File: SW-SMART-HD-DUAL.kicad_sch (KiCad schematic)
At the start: 52 parts, among them J1 SWD, J2 USART1, J3 PWRIN, SW1 BTS50010-1TAD, SW2 BTS50010-1TAD, U1 STM32G0B1KBTx, U3 LMR54410, U4 MCP2562

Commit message: lots of updates
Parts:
- CAN1: footprint TerminalBlock_TE-Connectivity:TerminalBlock_TE_282834-3_1x03_P2.54mm_Horizontal -> TerminalBlock_Phoenix:TerminalBlock_Phoenix_MPT-0,5-3-2.54_1x03_P2.54mm_Horizontal
- J3: footprint TerminalBlock_Phoenix:TerminalBlock_Phoenix_MKDS-3-2-5.08_1x02_P5.08mm_Horizontal -> TerminalBlock_Phoenix:TerminalBlock_Phoenix_MPT-0,5-2-2.54_1x02_P2.54mm_Horizontal
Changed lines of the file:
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@@
 			)
 		)
-		(property "Footprint" "TerminalBlock_TE-Connectivity:TerminalBlock_TE_282834-3_1x03_P2.54mm_Horizontal"
+		(property "Footprint" "TerminalBlock_Phoenix:TerminalBlock_Phoenix_MPT-0,5-3-2.54_1x03_P2.54mm_Horizontal"
 			(at 332.74 100.33 0)
 			(effects
@@
 			)
 		)
-		(property "Footprint" "TerminalBlock_Phoenix:TerminalBlock_Phoenix_MKDS-3-2-5.08_1x02_P5.08mm_Horizontal"
+		(property "Footprint" "TerminalBlock_Phoenix:TerminalBlock_Phoenix_MPT-0,5-2-2.54_1x02_P2.54mm_Horizontal"
 			(at 24.13 39.37 0)
 			(effects

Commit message: layout complete, drc passed
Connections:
- net SW1IS: now also U1.8 (PA1); no longer U1.7 (PA0)
- net SW2IS: now also U1.7 (PA0)
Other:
- moved on the sheet: POWER_OUT1
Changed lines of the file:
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@@
 	)
 	(junction
-		(at 198.12 153.67)
+		(at 160.02 153.67)
 		(diameter 0)
 		(color 0 0 0 0)
@@
 	)
 	(junction
-		(at 194.31 121.92)
+		(at 156.21 121.92)
 		(diameter 0)
 		(color 0 0 0 0)
@@
 	)
 	(junction
+		(at 160.02 133.35)
+		(diameter 0)
+		(color 0 0 0 0)
+	)
+	(junction
 		(at 299.72 160.02)
 		(diameter 0)
@@
 	)
 	(junction
-		(at 198.12 127)
-		(diameter 0)
-		(color 0 0 0 0)
-	)
-	(junction
 		(at 68.58 29.21)
 		(diameter 0)
@@
 	(wire
 		(pts
-			(xy 173.99 153.67) (xy 173.99 172.72)
+			(xy 160.02 153.67) (xy 160.02 172.72)
 		)
 		(stroke
@@
 	(wire
 		(pts
-			(xy 226.06 127) (xy 226.06 137.16)
+			(xy 187.96 127) (xy 187.96 137.16)
 		)
 		(stroke
@@
 	(wire
 		(pts
-			(xy 132.08 172.72) (xy 173.99 172.72)
-		)
-		(stroke
-			(width 0)
-			(type default)
-		)
-	)
-	(wire
-		(pts
 			(xy 302.26 139.7) (xy 290.83 139.7)
 		)
@@
 	(wire
 		(pts
+			(xy 289.56 48.26) (xy 293.37 48.26)
+		)
+		(stroke
+			(width 0)
+			(type default)
+		)
+	)
+	(wire
+		(pts
 			(xy 78.74 29.21) (xy 83.82 29.21)
 		)
@@
 	(wire
 		(pts
+			(xy 132.08 172.72) (xy 160.02 172.72)
+		)
+		(stroke
+			(width 0)
+			(type default)
+		)
+	)
+	(wire
+		(pts
 			(xy 62.23 21.59) (xy 53.34 21.59)
 		)
@@
 	(wire
 		(pts
-			(xy 228.6 139.7) (xy 228.6 121.92)
+			(xy 190.5 139.7) (xy 190.5 121.92)
 		)
 		(stroke
@@
 	(wire
 		(pts
-			(xy 194.31 116.84) (xy 194.31 121.92)
+			(xy 156.21 116.84) (xy 156.21 121.92)
 		)
 		(stroke
@@
 	(wire
 		(pts
-			(xy 223.52 153.67) (xy 223.52 142.24)
+			(xy 185.42 153.67) (xy 185.42 142.24)
 		)
 		(stroke
@@
 	(wire
 		(pts
-			(xy 220.98 139.7) (xy 228.6 139.7)
+			(xy 182.88 139.7) (xy 190.5 139.7)
 		)
 		(stroke
@@
 	(wire
 		(pts
+			(xy 160.02 133.35) (xy 160.02 127)
+		)
+		(stroke
+			(width 0)
+			(type default)
+		)
+	)
+	(wire
+		(pts
 			(xy 226.06 53.34) (xy 226.06 57.15)
 		)
@@
 	(wire
 		(pts
-			(xy 220.98 137.16) (xy 226.06 137.16)
+			(xy 182.88 137.16) (xy 187.96 137.16)
 		)
 		(stroke
@@
 	(wire
 		(pts
-			(xy 137.16 133.35) (xy 160.02 133.35)
-		)
-		(stroke
-			(width 0)
-			(type default)
-		)
-	)
-	(wire
-		(pts
 			(xy 68.58 35.56) (xy 68.58 60.96)
 		)
@@
 	(wire
 		(pts
-			(xy 198.12 142.24) (xy 198.12 153.67)
-		)
-		(stroke
-			(width 0)
-			(type default)
-		)
-	)
-	(wire
-		(pts
-			(xy 160.02 127) (xy 198.12 127)
+			(xy 160.02 142.24) (xy 160.02 153.67)
 		)
 		(stroke
@@
 	(wire
 		(pts
-			(xy 198.12 137.16) (xy 200.66 137.16)
+			(xy 160.02 137.16) (xy 162.56 137.16)
 		)
 		(stroke
@@
 	(wire
 		(pts
-			(xy 160.02 127) (xy 160.02 133.35)
-		)
-		(stroke
-			(width 0)
-			(type default)
-		)
-	)
-	(wire
-		(pts
 			(xy 289.56 78.74) (xy 293.37 78.74)
 		)
@@
 	(wire
 		(pts
-			(xy 173.99 153.67) (xy 198.12 153.67)
-		)
-		(stroke
-			(width 0)
-			(type default)
-		)
-	)
-	(wire
-		(pts
 			(xy 67.31 80.01) (xy 69.85 80.01)
 		)
@@
 	(wire
 		(pts
-			(xy 194.31 139.7) (xy 200.66 139.7)
+			(xy 156.21 139.7) (xy 162.56 139.7)
 		)
 		(stroke
@@
 	(wire
 		(pts
-			(xy 198.12 127) (xy 226.06 127)
+			(xy 160.02 127) (xy 187.96 127)
 		)
 		(stroke
@@
 	(wire
 		(pts
-			(xy 194.31 121.92) (xy 194.31 139.7)
+			(xy 156.21 121.92) (xy 156.21 139.7)
 		)
 		(stroke
@@
 	(wire
 		(pts
-			(xy 198.12 142.24) (xy 200.66 142.24)
+			(xy 160.02 142.24) (xy 162.56 142.24)
 		)
 		(stroke
@@
 	(wire
 		(pts
+			(xy 137.16 133.35) (xy 160.02 133.35)
+		)
+		(stroke
+			(width 0)
+			(type default)
+		)
+	)
+	(wire
+		(pts
 			(xy 46.99 128.27) (xy 52.07 128.27)
 		)
@@
 	(wire
 		(pts
-			(xy 220.98 142.24) (xy 223.52 142.24)
+			(xy 182.88 142.24) (xy 185.42 142.24)
 		)
 		(stroke
@@
 	(wire
 		(pts
-			(xy 198.12 153.67) (xy 223.52 153.67)
+			(xy 160.02 153.67) (xy 185.42 153.67)
 		)
 		(stroke
@@
 	(wire
 		(pts
-			(xy 198.12 137.16) (xy 198.12 127)
+			(xy 160.02 137.16) (xy 160.02 133.35)
 		)
 		(stroke
@@
 	(wire
 		(pts
-			(xy 228.6 121.92) (xy 194.31 121.92)
+			(xy 190.5 121.92) (xy 156.21 121.92)
 		)
 		(stroke
@@
 		)
 	)
-	(label "SW2OUT"
-		(at 173.99 157.48 0)
-		(effects
-			(font
-				(size 1.27 1.27)
-			)
-			(justify left bottom)
-		)
-	)
 	(label "SW"
 		(at 68.58 90.17 0)
@@
 	)
 	(label "SW1IS"
-		(at 293.37 45.72 0)
+		(at 293.37 48.26 0)
 		(effects
 			(font
@@
 		)
 	)
+	(label "SW2IS"
+		(at 293.37 45.72 0)
+		(effects
+			(font
+				(size 1.27 1.27)
+			)
+			(justify left bottom)
+		)
+	)
 	(label "SW1IS"
 		(at 46.99 138.43 180)
@@
 			)
 		)
-		(property "Datasheet" "https://www.infineon.com/dgdl/Infineon-BTS50010-1TAD-DS-v01_00-EN.pdf?fileId=5546d462576f34750157c38810ca55cd"
+		(property "Datasheet" "https://www.infineon.com/assets/row/public/documents/10/49/infineon-bts50010-1tad-datasheet-en.pdf"
 			(at 85.09 182.88 0)
 			(effects
@@
 			)
 		)
-		(property "Datasheet" "https://www.infineon.com/dgdl/Infineon-BTS50010-1TAD-DS-v01_00-EN.pdf?fileId=5546d462576f34750157c38810ca55cd"
+		(property "Datasheet" "https://www.infineon.com/assets/row/public/documents/10/49/infineon-bts50010-1tad-datasheet-en.pdf"
 			(at 90.17 143.51 0)
 			(effects
@@
 	(symbol
 		(lib_id "power:+12V")
-		(at 194.31 116.84 0)
+		(at 156.21 116.84 0)
 		(unit 1)
 		(exclude_from_sim no)
@@
 		(fields_autoplaced yes)
 		(property "Reference" "#PWR07"
-			(at 194.31 120.65 0)
+			(at 156.21 120.65 0)
 			(effects
 				(font
@@
 		)
 		(property "Value" "+12V"
-			(at 194.31 111.76 0)
+			(at 156.21 111.76 0)
 			(effects
 				(font
@@
 		)
 		(property "Footprint" ""
-			(at 194.31 116.84 0)
+			(at 156.21 116.84 0)
 			(effects
 				(font
@@
 		)
 		(property "Datasheet" ""
-			(at 194.31 116.84 0)
+			(at 156.21 116.84 0)
 			(effects
 				(font
@@
 		)
 		(property "Description" "Power symbol creates a global label with name \"+12V\""
-			(at 194.31 116.84 0)
+			(at 156.21 116.84 0)
 			(effects
 				(font
@@
 	(symbol
 		(lib_id "SamacSys_Parts:VP0365840000G")
-		(at 220.98 142.24 180)
+		(at 182.88 142.24 180)
 		(unit 1)
 		(exclude_from_sim no)
@@
 		(fields_autoplaced yes)
 		(property "Reference" "POWER_OUT1"
-			(at 210.82 129.54 0)
+			(at 172.72 129.54 0)
 			(effects
 				(font
@@
 		)
 		(property "Value" "VP0365840000G"
-			(at 210.82 132.08 0)
+			(at 172.72 132.08 0)
 			(effects
 				(font
@@
 		)
 		(property "Footprint" "VP0365840000G"
-			(at 204.47 47.32 0)
+			(at 166.37 47.32 0)
 			(effects
 				(font
@@
 		)
 		(property "Datasheet" "https://www.mouser.ca/ProductDetail/Amphenol-Anytek/VP0365840000G?qs=Mv7BduZupUgzoCVpYg1nQw%3D%3D"
-			(at 204.47 -52.68 0)
+			(at 166.37 -52.68 0)
 			(effects
 				(font
@@
 		)
 		(property "Description" "3 Position Wire to Board Terminal Block Horizontal with Board 0.400\" (10.16mm) Through Hole"
-			(at 220.98 142.24 0)
+			(at 182.88 142.24 0)
 			(effects
 				(font
@@
 		)
 		(property "Height" "28.8"
-			(at 204.47 -252.68 0)
+			(at 166.37 -252.68 0)
 			(effects
 				(font
@@
 		)
 		(property "Mouser Part Number" "649-VP03658400J0G"
-			(at 204.47 -352.68 0)
+			(at 166.37 -352.68 0)
 			(effects
 				(font
@@
 		)
 		(property "Mouser Price/Stock" "https://www.mouser.co.uk/ProductDetail/Amphenol-Anytek/VP0365840000G?qs=Mv7BduZupUgzoCVpYg1nQw%3D%3D"
-			(at 204.47 -452.68 0)
+			(at 166.37 -452.68 0)
 			(effects
 				(font
@@
 		)
 		(property "Manufacturer_Name" "Amphenol"
-			(at 204.47 -552.68 0)
+			(at 166.37 -552.68 0)
 			(effects
 				(font
@@
 		)
 		(property "Manufacturer_Part_Number" "VP0365840000G"
-			(at 204.47 -652.68 0)
+			(at 166.37 -652.68 0)
 			(effects
 				(font

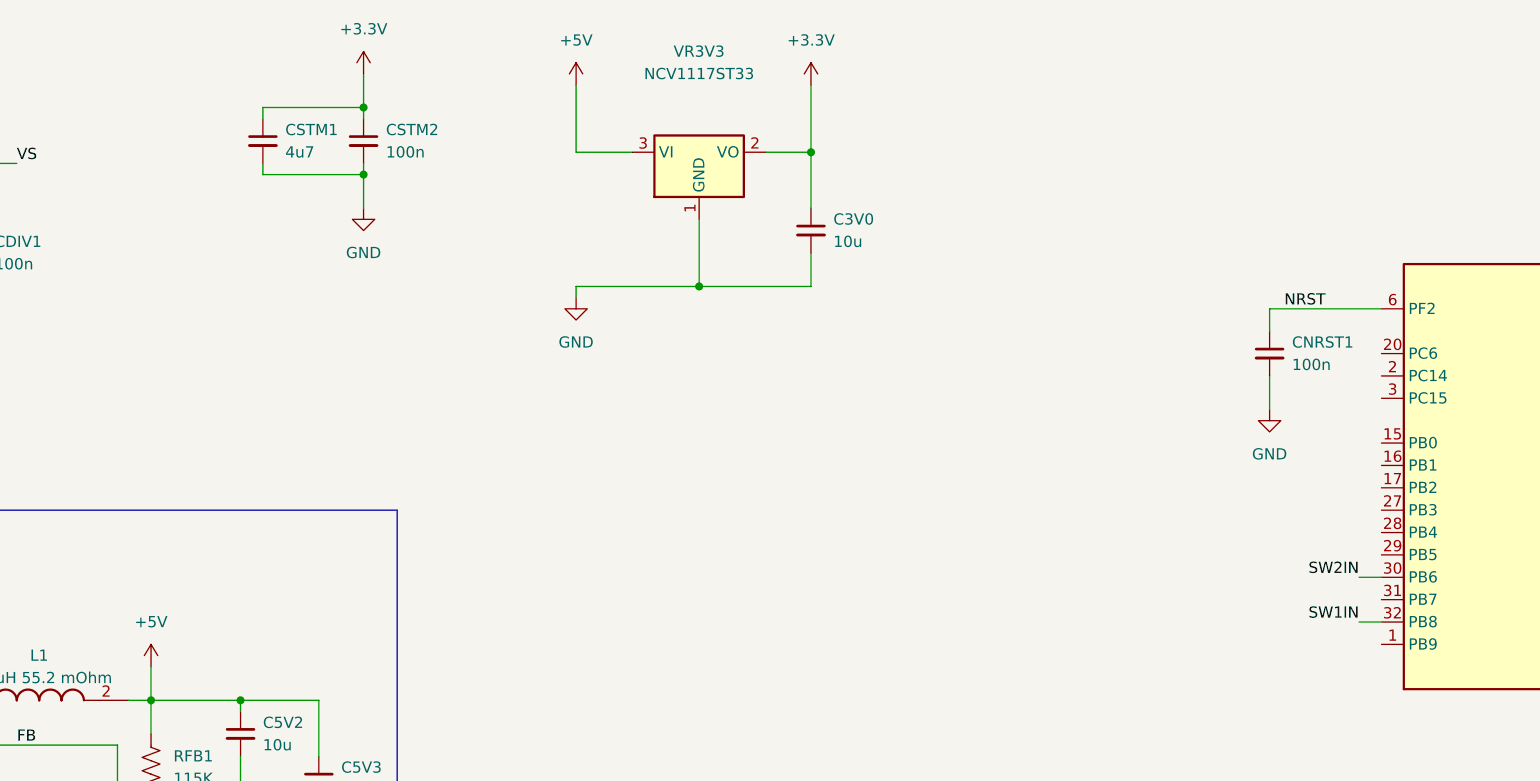
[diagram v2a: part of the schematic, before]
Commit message: added crystal osc, fixed some silkscreen issues, moved a few tracks
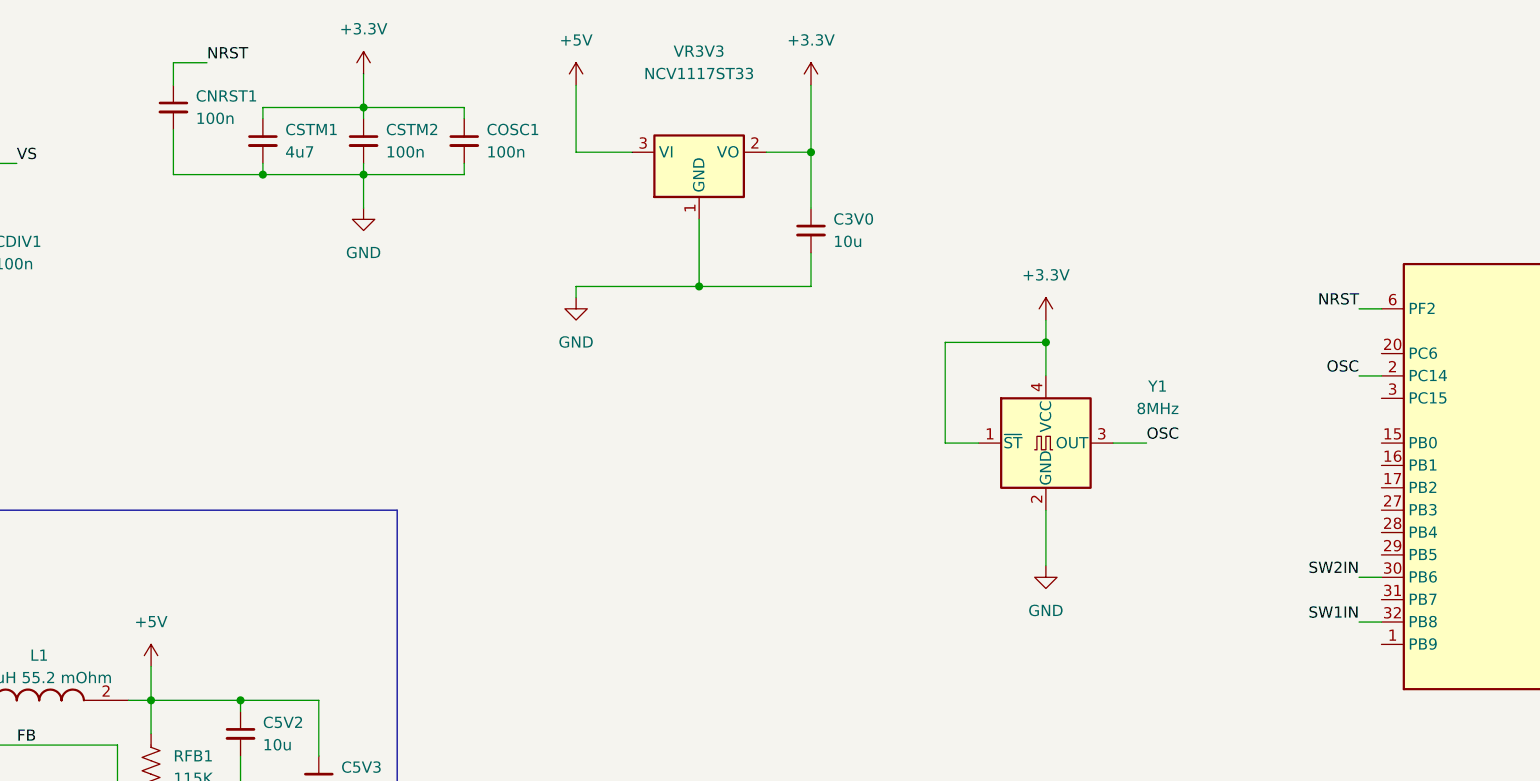
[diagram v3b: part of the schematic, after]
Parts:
- added COSC1: 100n, Capacitor_SMD:C_0603_1608Metric_Pad1.08x0.95mm_HandSolder, symbol Device:C_Small
- added Y1: 8MHz, Oscillator:Oscillator_SMD_EuroQuartz_XO32-4Pin_3.2x2.5mm_RotB_HandSoldering, symbol Oscillator:SG-5032CAN
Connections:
- net +3.3V: now also COSC1.1, Y1.1 (~{ST}), Y1.4 (VCC)
- net GND: now also COSC1.2, Y1.2 (GND)
- net OSC: now reaches U1.2 (PC14)
- net OSC: now also Y1.3 (OUT)
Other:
- moved on the sheet: CNRST1
